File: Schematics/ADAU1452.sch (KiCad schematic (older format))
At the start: 98 parts, among them CN201 COAX, P201 CONN_2x1, P202 CONN_2x1, P203 CONN_6X2, P204 CONN_6x1, SW201 SWITCH, SW202 SWITCH, U201 ADAU1452WBCPZ, U202 ADM13307-5ARZ, U203 25AA1024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

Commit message: Footprint changes
Footprint changes
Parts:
- R217: footprint OHDSP-Footprints-Pretty:SMD-0805 -> OHDSP-Footprints-Pretty:SMD-0603
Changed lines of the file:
@@
 F 0 "R217" V 6400 7750 40  0000 C CNN
 F 1 "4k3" V 6357 7451 40  0000 C CNN
-F 2 "OHDSP-Footprints-Pretty:SMD-0805" V 6280 7450 30  0001 C CNN
+F 2 "OHDSP-Footprints-Pretty:SMD-0603" V 6280 7450 30  0001 C CNN
 F 3 "~" H 6350 7450 30  0000 C CNN
 	1    6350 7450

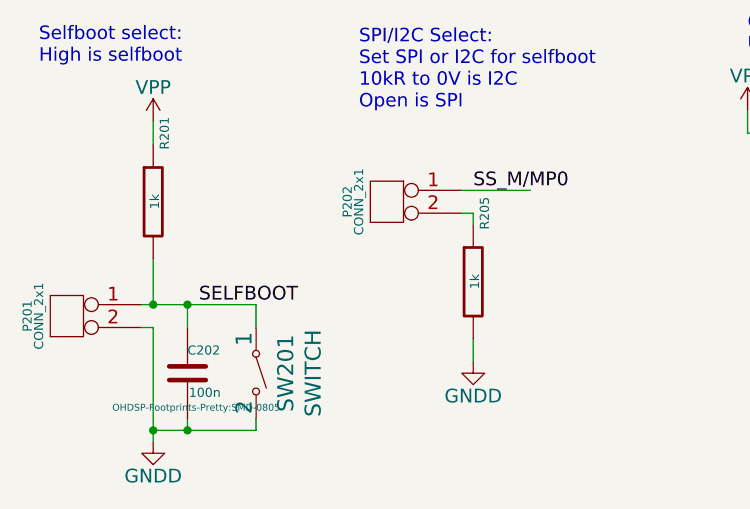
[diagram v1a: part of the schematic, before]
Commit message: PCB changes, minor schematic changes
Removed switch on selfboot pin, as it has a jumper anyway... Removed
SPI/I2C jumper for selfboot as sticking with serial EEPROM. Changed some
component footprints (R207 to R216 0603 to 0805).
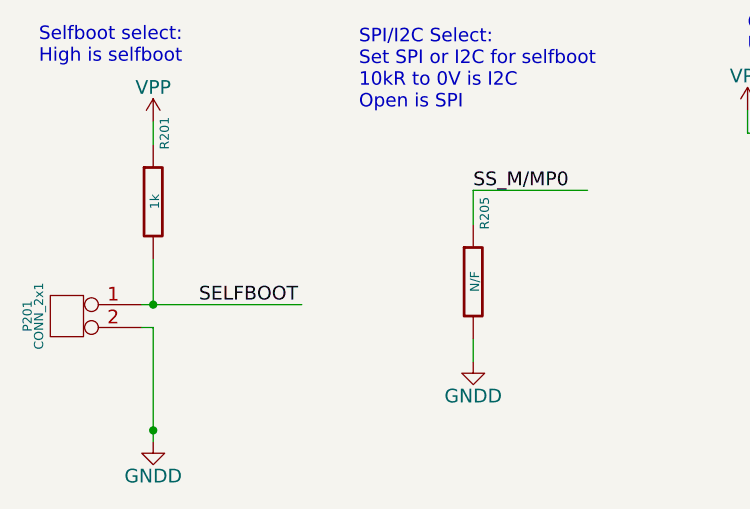
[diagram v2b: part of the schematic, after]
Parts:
- removed C202: 100n, OHDSP-Footprints-Pretty:SMD-0805, symbol C
- removed P202: CONN_2x1, OHDSP-Footprints-Pretty:CONN_SIL_2, symbol CONN_2x1
- removed SW201: SWITCH, OHDSP-Footprints-Pretty:SW_TACT_TH, symbol SWITCH
- R205: value 1k -> N/F
- R207, R208, R209, R210, R211, R212, R213, R214, R215, R216: footprint OHDSP-Footprints-Pretty:SMD-0603 -> OHDSP-Footprints-Pretty:SMD-0805
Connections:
- wire segments 323 -> 317

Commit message: PCB Work
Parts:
- added C202: 220u, OHDSP-Footprints-Pretty:CAP-TH-D6.3mmP2.5mm, symbol CP1
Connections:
- wire segments 317 -> 318
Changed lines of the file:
@@
 Connection ~ 15000 1050
 Wire Wire Line
-	13150 900  13150 1050
+	13150 900  13150 1300
 Wire Wire Line
 	13150 1050 13250 1050
@@
 	1150 10250 1850 10250
 Connection ~ 1200 10250
+$Comp
+L CP1 C202
+U 1 1 54F4BBFB
+P 13150 1500
+F 0 "C202" H 13200 1600 50  0000 L CNN
+F 1 "220u" H 13200 1400 50  0000 L CNN
+F 2 "OHDSP-Footprints-Pretty:CAP-TH-D6.3mmP2.5mm" H 13150 1500 60  0000 C CNN
+F 3 "~" H 13150 1500 60  0000 C CNN
+	1    13150 1500
+	1    0    0    -1
+$EndComp
+$Comp
+L GNDD #PWR039
+U 1 1 54F4C05D
+P 13150 1750
+F 0 "#PWR039" H 13150 1500 60  0001 C CNN
+F 1 "GNDD" H 13150 1600 60  0000 C CNN
+F 2 "" H 13150 1750 60  0000 C CNN
+F 3 "" H 13150 1750 60  0000 C CNN
+	1    13150 1750
+	1    0    0    -1
+$EndComp
+Wire Wire Line
+	13150 1750 13150 1700
+Connection ~ 13150 1050
 $EndSCHEMATC

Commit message: PCB Work, change reset switch to SMD
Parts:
- SW202: footprint OHDSP-Footprints-Pretty:SW_TACT_TH -> OHDSP-Footprints-Pretty:SW_TACT_SMD
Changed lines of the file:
@@
 F 0 "SW202" H 9550 10230 70  0000 C CNN
 F 1 "SWITCH" H 9550 10350 70  0000 C CNN
-F 2 "OHDSP-Footprints-Pretty:SW_TACT_TH" H 9615 10100 60  0001 C CNN
+F 2 "OHDSP-Footprints-Pretty:SW_TACT_SMD" H 9615 10100 60  0001 C CNN
 F 3 "" H 9615 10100 60  0000 C CNN
 	1    9350 10100

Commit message: PCB Work, minor schematic changes
Removed cap and LED, changed one net label
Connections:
- net labels removed: SS_M/MP0
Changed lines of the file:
@@
 	1    0    0    -1
 $EndComp
-Text Label 2600 9750 0    60   ~ 0
-SS_M/MP0
 Text Notes 2100 9400 0    59   ~ 0
 SPI/I2C Select:\nSet SPI or I2C for selfboot\n10kR to 0V is I2C\nOpen is SPI
@@
 	13150 1750 13150 1700
 Connection ~ 13150 1050
+Text Label 2900 9750 0    60   ~ 0
+M_SS
 $EndSCHEMATC

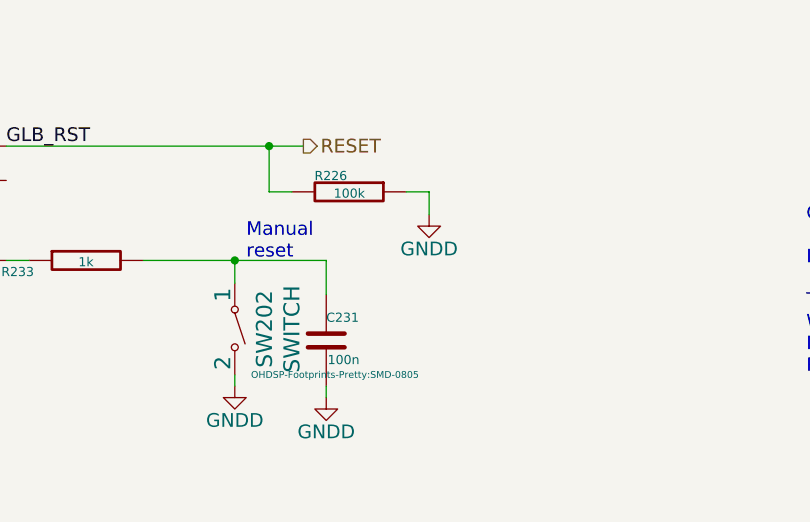
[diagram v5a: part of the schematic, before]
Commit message: PCB work, added manual reset to Pi header
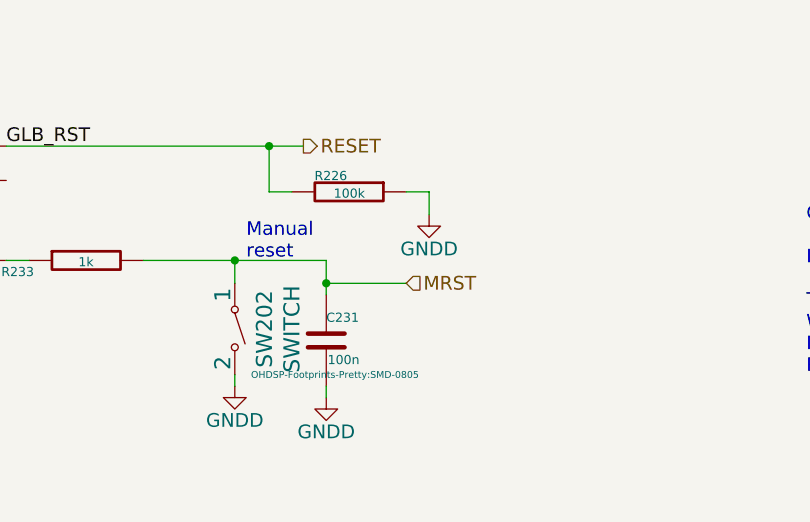
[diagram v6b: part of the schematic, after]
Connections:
- net labels added: MRST
- wire segments 318 -> 319
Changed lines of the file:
@@
 Text Label 2900 9750 0    60   ~ 0
 M_SS
+Text HLabel 10100 10100 2    60   Input ~ 0
+MRST
+Wire Wire Line
+	10100 10100 9750 10100
+Connection ~ 9750 10100
 $EndSCHEMATC

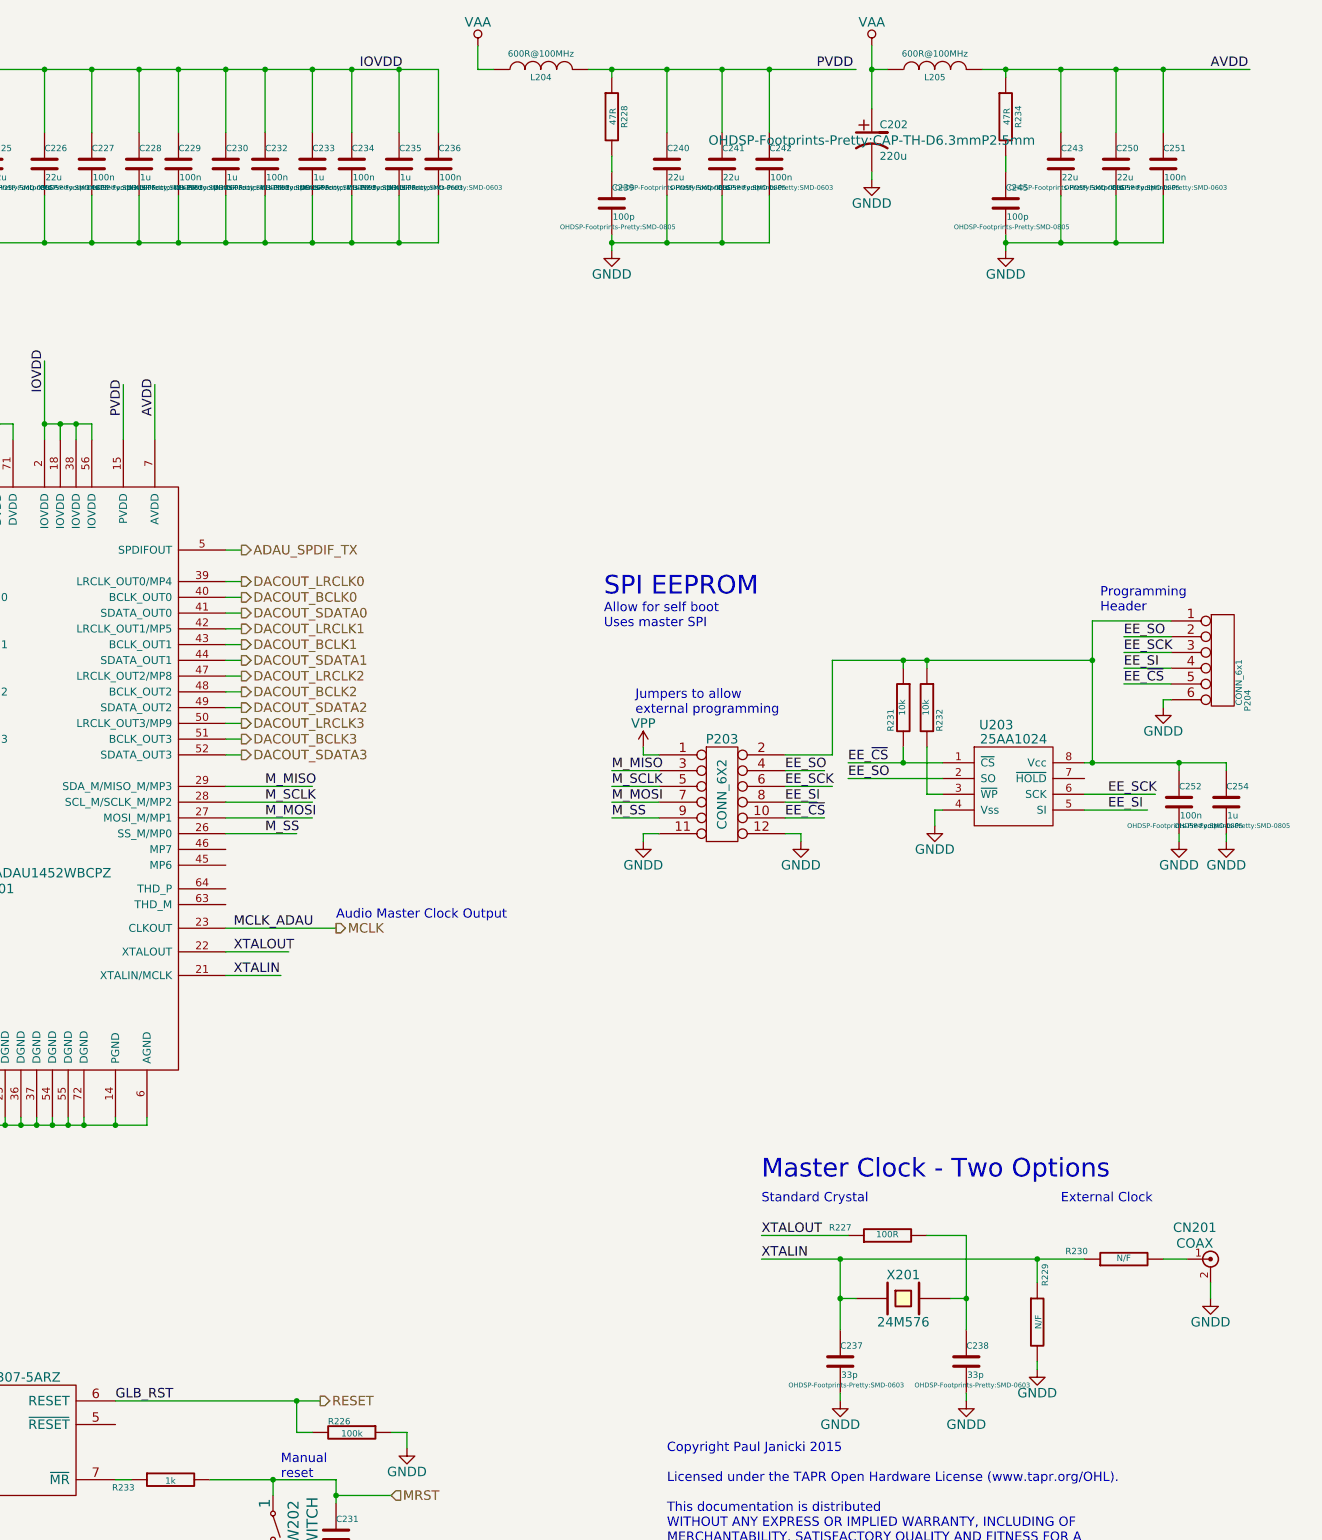
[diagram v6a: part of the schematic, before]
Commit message: PCB work, Running Electrical Rule Check
PCB work, Running Electrical Rule Check:
Added no connects to schematics, added missing pull up on EEPROM, remove
USB_CLK/USB_RESET label on USB/I2C header and added NC. Minor change on
Pi connectors.
Removed old large PCB file.
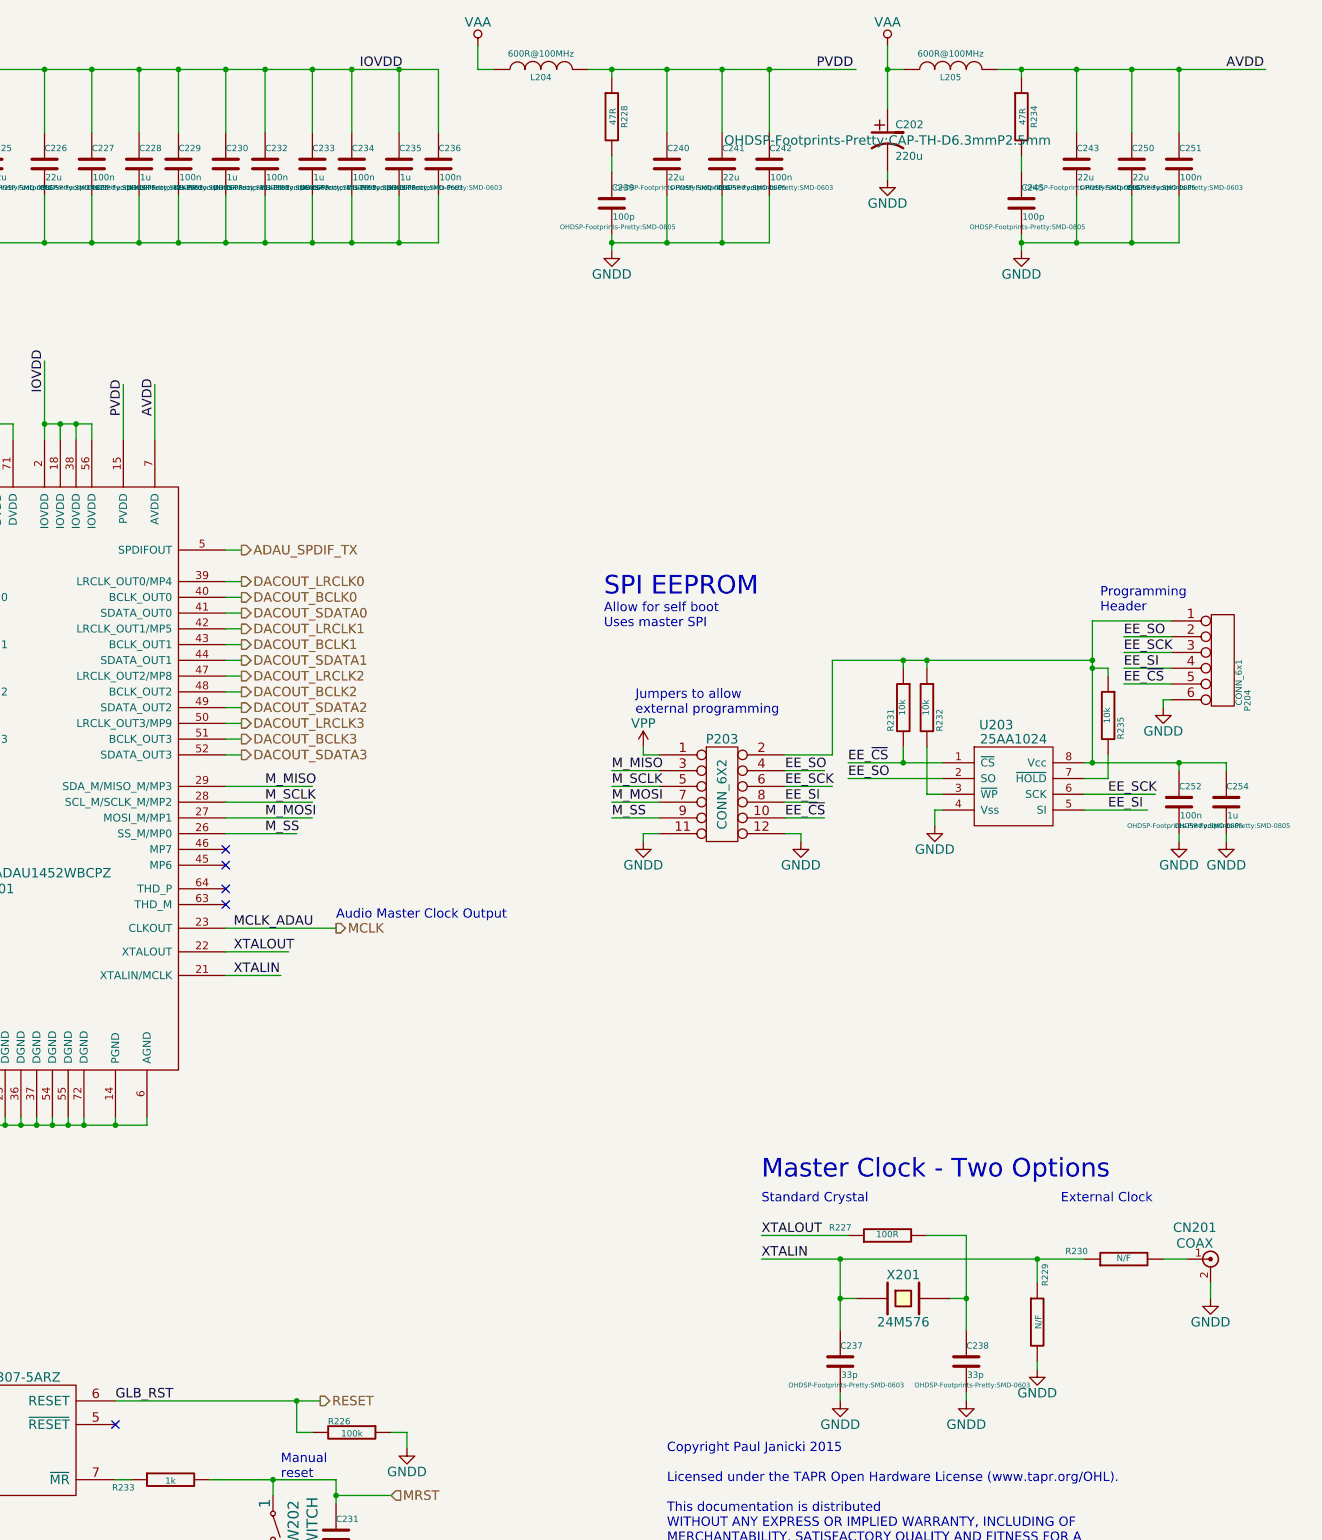
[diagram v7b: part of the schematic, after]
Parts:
- added R235: 10k, OHDSP-Footprints-Pretty:SMD-0805, symbol R
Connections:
- wire segments 319 -> 323
- no-connect marks 0 -> 5
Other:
- moved on the sheet: C202, C243, C245, C250, C251, L205, R234
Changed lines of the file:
@@
 L VAA #PWR07
 U 1 1 54DB3C56
-P 13150 900
-F 0 "#PWR07" H 13150 750 60  0001 C CNN
-F 1 "VAA" H 13150 1050 60  0000 C CNN
-F 2 "" H 13150 900 60  0000 C CNN
-F 3 "" H 13150 900 60  0000 C CNN
-	1    13150 900
+P 13250 900
+F 0 "#PWR07" H 13250 750 60  0001 C CNN
+F 1 "VAA" H 13250 1050 60  0000 C CNN
+F 2 "" H 13250 900 60  0000 C CNN
+F 3 "" H 13250 900 60  0000 C CNN
+	1    13250 900
 	1    0    0    -1
 $EndComp
@@
 L INDUCTOR L205
 U 1 1 54DB3C5C
-P 13550 1050
-F 0 "L205" V 13500 1050 40  0000 C CNN
-F 1 "600R@100MHz" V 13650 1050 40  0000 C CNN
-F 2 "OHDSP-Footprints-Pretty:SMD-0805" H 13550 1050 60  0001 C CNN
-F 3 "~" H 13550 1050 60  0000 C CNN
-	1    13550 1050
+P 13650 1050
+F 0 "L205" V 13600 1050 40  0000 C CNN
+F 1 "600R@100MHz" V 13750 1050 40  0000 C CNN
+F 2 "OHDSP-Footprints-Pretty:SMD-0805" H 13650 1050 60  0001 C CNN
+F 3 "~" H 13650 1050 60  0000 C CNN
+	1    13650 1050
 	0    -1   -1   0
 $EndComp
@@
 L C C245
 U 1 1 54DB3C62
-P 14000 1900
-F 0 "C245" H 14000 2000 40  0000 L CNN
-F 1 "100p" H 14006 1815 40  0000 L CNN
-F 2 "OHDSP-Footprints-Pretty:SMD-0805" H 14038 1750 30  0000 C CNN
-F 3 "~" H 14000 1900 60  0000 C CNN
-	1    14000 1900
+P 14100 1900
+F 0 "C245" H 14100 2000 40  0000 L CNN
+F 1 "100p" H 14106 1815 40  0000 L CNN
+F 2 "OHDSP-Footprints-Pretty:SMD-0805" H 14138 1750 30  0000 C CNN
+F 3 "~" H 14100 1900 60  0000 C CNN
+	1    14100 1900
 	1    0    0    -1
 $EndComp
@@
 L R R234
 U 1 1 54DB3C68
-P 14000 1350
-F 0 "R234" V 14080 1350 40  0000 C CNN
-F 1 "47R" V 14007 1351 40  0000 C CNN
-F 2 "OHDSP-Footprints-Pretty:SMD-0805" V 13930 1350 30  0001 C CNN
-F 3 "~" H 14000 1350 30  0000 C CNN
-	1    14000 1350
+P 14100 1350
+F 0 "R234" V 14180 1350 40  0000 C CNN
+F 1 "47R" V 14107 1351 40  0000 C CNN
+F 2 "OHDSP-Footprints-Pretty:SMD-0805" V 14030 1350 30  0001 C CNN
+F 3 "~" H 14100 1350 30  0000 C CNN
+	1    14100 1350
 	1    0    0    -1
 $EndComp
@@
 L GNDD #PWR08
 U 1 1 54DB3C77
-P 14000 2200
-F 0 "#PWR08" H 14000 1950 60  0001 C CNN
-F 1 "GNDD" H 14000 2050 60  0000 C CNN
-F 2 "" H 14000 2200 60  0000 C CNN
-F 3 "" H 14000 2200 60  0000 C CNN
-	1    14000 2200
+P 14100 2200
+F 0 "#PWR08" H 14100 1950 60  0001 C CNN
+F 1 "GNDD" H 14100 2050 60  0000 C CNN
+F 2 "" H 14100 2200 60  0000 C CNN
+F 3 "" H 14100 2200 60  0000 C CNN
+	1    14100 2200
 	1    0    0    -1
 $EndComp
@@
 L C C251
 U 1 1 54DB3C8F
-P 15000 1650
-F 0 "C251" H 15000 1750 40  0000 L CNN
-F 1 "100n" H 15006 1565 40  0000 L CNN
-F 2 "OHDSP-Footprints-Pretty:SMD-0603" H 15038 1500 30  0000 C CNN
-F 3 "~" H 15000 1650 60  0000 C CNN
-	1    15000 1650
+P 15100 1650
+F 0 "C251" H 15100 1750 40  0000 L CNN
+F 1 "100n" H 15106 1565 40  0000 L CNN
+F 2 "OHDSP-Footprints-Pretty:SMD-0603" H 15138 1500 30  0000 C CNN
+F 3 "~" H 15100 1650 60  0000 C CNN
+	1    15100 1650
 	1    0    0    -1
 $EndComp
@@
 L C C250
 U 1 1 54DB3C95
-P 14700 1650
-F 0 "C250" H 14700 1750 40  0000 L CNN
-F 1 "22u" H 14706 1565 40  0000 L CNN
-F 2 "OHDSP-Footprints-Pretty:SMD-0805" H 14738 1500 30  0000 C CNN
-F 3 "~" H 14700 1650 60  0000 C CNN
-	1    14700 1650
-	1    0    0    -1
-$EndComp
-Text Label 15300 1050 0    60   ~ 0
+P 14800 1650
+F 0 "C250" H 14800 1750 40  0000 L CNN
+F 1 "22u" H 14806 1565 40  0000 L CNN
+F 2 "OHDSP-Footprints-Pretty:SMD-0805" H 14838 1500 30  0000 C CNN
+F 3 "~" H 14800 1650 60  0000 C CNN
+	1    14800 1650
+	1    0    0    -1
+$EndComp
+Text Label 15400 1050 0    60   ~ 0
 AVDD
 Text Label 8600 3250 1    60   ~ 0
@@
 L C C243
 U 1 1 54F127C8
-P 14350 1650
-F 0 "C243" H 14350 1750 40  0000 L CNN
-F 1 "22u" H 14356 1565 40  0000 L CNN
-F 2 "OHDSP-Footprints-Pretty:SMD-0805" H 14388 1500 30  0000 C CNN
-F 3 "~" H 14350 1650 60  0000 C CNN
-	1    14350 1650
+P 14450 1650
+F 0 "C243" H 14450 1750 40  0000 L CNN
+F 1 "22u" H 14456 1565 40  0000 L CNN
+F 2 "OHDSP-Footprints-Pretty:SMD-0805" H 14488 1500 30  0000 C CNN
+F 3 "~" H 14450 1650 60  0000 C CNN
+	1    14450 1650
 	1    0    0    -1
 $EndComp
@@
 	10650 1050 10750 1050
 Wire Wire Line
-	13850 1050 15550 1050
-Wire Wire Line
-	14000 1050 14000 1100
-Wire Wire Line
-	14000 1600 14000 1700
-Wire Wire Line
-	14350 1050 14350 1450
-Connection ~ 14000 1050
-Wire Wire Line
-	14700 1050 14700 1450
-Connection ~ 14350 1050
-Connection ~ 14700 1050
-Wire Wire Line
-	14000 2100 14000 2200
-Wire Wire Line
-	14350 2150 14350 1850
-Connection ~ 14000 2150
-Wire Wire Line
-	14700 2150 14700 1850
-Connection ~ 14350 2150
-Connection ~ 14700 2150
-Wire Wire Line
-	15000 1050 15000 1450
-Wire Wire Line
-	15000 2150 15000 1850
-Connection ~ 15000 1050
-Wire Wire Line
-	13150 900  13150 1300
-Wire Wire Line
-	13150 1050 13250 1050
+	13950 1050 15650 1050
+Wire Wire Line
+	14100 1050 14100 1100
+Wire Wire Line
+	14100 1600 14100 1700
+Wire Wire Line
+	14450 1050 14450 1450
+Connection ~ 14100 1050
+Wire Wire Line
+	14800 1050 14800 1450
+Connection ~ 14450 1050
+Connection ~ 14800 1050
+Wire Wire Line
+	14100 2100 14100 2200
+Wire Wire Line
+	14450 2150 14450 1850
+Connection ~ 14100 2150
+Wire Wire Line
+	14800 2150 14800 1850
+Connection ~ 14450 2150
+Connection ~ 14800 2150
+Wire Wire Line
+	15100 1050 15100 1450
+Wire Wire Line
+	15100 2150 15100 1850
+Connection ~ 15100 1050
+Wire Wire Line
+	13250 900  13250 1300
+Wire Wire Line
+	13250 1050 13350 1050
 Wire Wire Line
 	8400 3400 8400 3050
@@
 	6650 7000 6750 7000
 Wire Wire Line
-	14000 2150 15000 2150
+	14100 2150 15100 2150
 Wire Wire Line
 	11500 2150 12500 2150
@@
 L CP1 C202
 U 1 1 54F4BBFB
-P 13150 1500
-F 0 "C202" H 13200 1600 50  0000 L CNN
-F 1 "220u" H 13200 1400 50  0000 L CNN
-F 2 "OHDSP-Footprints-Pretty:CAP-TH-D6.3mmP2.5mm" H 13150 1500 60  0000 C CNN
-F 3 "~" H 13150 1500 60  0000 C CNN
-	1    13150 1500
+P 13250 1500
+F 0 "C202" H 13300 1600 50  0000 L CNN
+F 1 "220u" H 13300 1400 50  0000 L CNN
+F 2 "OHDSP-Footprints-Pretty:CAP-TH-D6.3mmP2.5mm" H 13250 1500 60  0000 C CNN
+F 3 "~" H 13250 1500 60  0000 C CNN
+	1    13250 1500
 	1    0    0    -1
 $EndComp
@@
 L GNDD #PWR039
 U 1 1 54F4C05D
-P 13150 1750
-F 0 "#PWR039" H 13150 1500 60  0001 C CNN
-F 1 "GNDD" H 13150 1600 60  0000 C CNN
-F 2 "" H 13150 1750 60  0000 C CNN
-F 3 "" H 13150 1750 60  0000 C CNN
-	1    13150 1750
-	1    0    0    -1
-$EndComp
-Wire Wire Line
-	13150 1750 13150 1700
-Connection ~ 13150 1050
+P 13250 1750
+F 0 "#PWR039" H 13250 1500 60  0001 C CNN
+F 1 "GNDD" H 13250 1600 60  0000 C CNN
+F 2 "" H 13250 1750 60  0000 C CNN
+F 3 "" H 13250 1750 60  0000 C CNN
+	1    13250 1750
+	1    0    0    -1
+$EndComp
+Wire Wire Line
+	13250 1750 13250 1700
+Connection ~ 13250 1050
 Text Label 2900 9750 0    60   ~ 0
 M_SS
@@
 	10100 10100 9750 10100
 Connection ~ 9750 10100
+NoConn ~ 9050 6000
+NoConn ~ 9050 6100
+NoConn ~ 9050 6250
+NoConn ~ 9050 6350
+NoConn ~ 8350 9650
+$Comp
+L R R235
+U 1 1 54FFE001
+P 14650 5150
+F 0 "R235" V 14570 5070 40  0000 C CNN
+F 1 "10k" V 14657 5151 40  0000 C CNN
+F 2 "OHDSP-Footprints-Pretty:SMD-0805" V 14580 5150 30  0001 C CNN
+F 3 "~" H 14650 5150 30  0000 C CNN
+	1    14650 5150
+	-1   0    0    -1
+$EndComp
+Connection ~ 14550 4850
+Wire Wire Line
+	14550 4850 14650 4850
+Wire Wire Line
+	14650 4850 14650 4900
+Wire Wire Line
+	14650 5400 14650 5550
+Wire Wire Line
+	14650 5550 14500 5550
 $EndSCHEMATC
